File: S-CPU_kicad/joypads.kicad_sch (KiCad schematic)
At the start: 280 parts, among them U33 OR_2, U38 OR_2

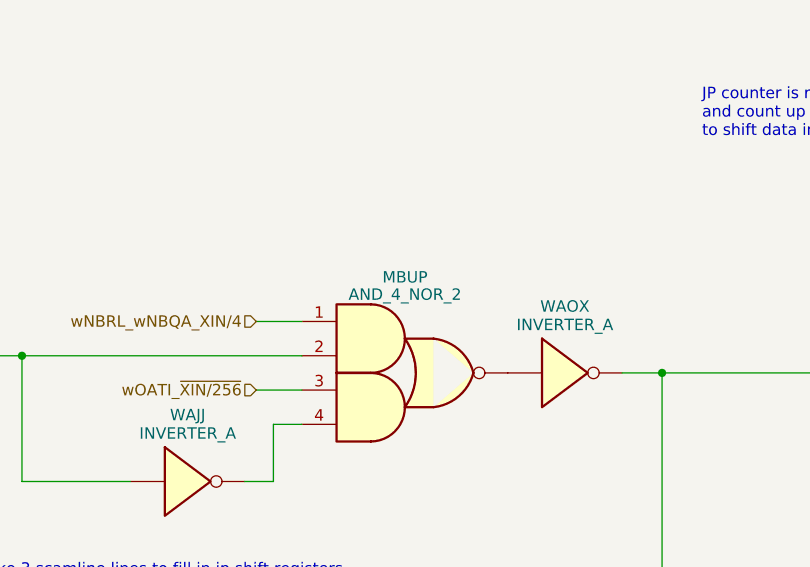
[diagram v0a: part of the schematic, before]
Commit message: Fixed complex gate names. Most fo the cells in the mul div section have been idnetified in SVG file.
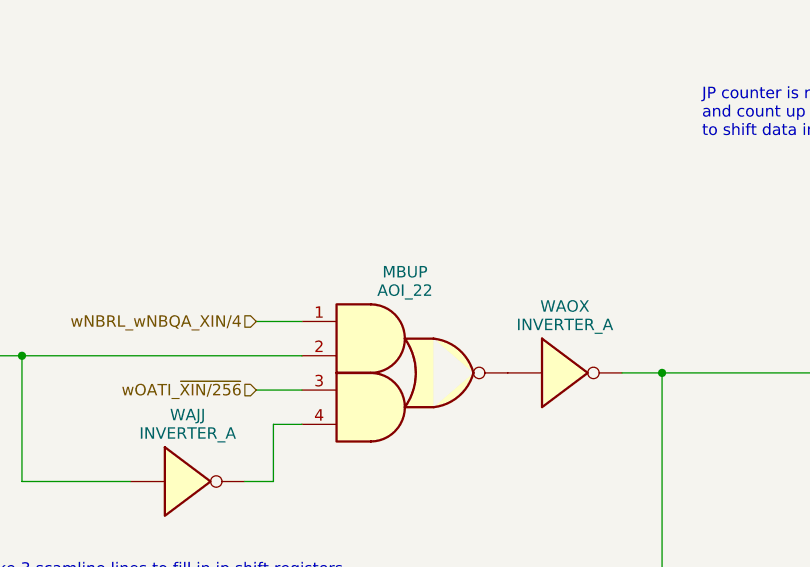
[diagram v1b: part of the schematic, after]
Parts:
- MBUP: value AND_4_NOR_2 -> AOI_22; symbol Ricoh_Cells:AND_2_AND_2_NOR_2 -> Ricoh_Cells:AOI_22
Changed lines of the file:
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@@
     )
   )
-  (symbol (lib_id "Ricoh_Cells:AND_2_AND_2_NOR_2") (at 226.06 92.71 0) (unit 1)
+  (symbol (lib_id "Ricoh_Cells:AOI_22") (at 226.06 92.71 0) (unit 1)
     (in_bom yes) (on_board yes) (dnp no) (fields_autoplaced)
-    (property "Reference" "MBUP" (at 229.8837 80.8101 0)
+    (property "Reference" "MBUP" (at 229.8837 80.24 0)
       (effects (font (size 1.27 1.27)))
     )
-    (property "Value" "AND_4_NOR_2" (at 229.8837 82.7311 0)
+    (property "Value" "AOI_22" (at 229.8837 82.288 0)
       (effects (font (size 1.27 1.27)))
     )
@@
         )
         (path "/ca9d3ca9-0297-4b98-a109-b7c162ccc5c3/c42cdb83-bc69-486b-820b-017180bd7612"
-          (reference "MBUP1") (unit 1)
+          (reference "WAMB") (unit 1)
         )
       )

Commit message: More MUL DIV section updates,
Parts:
- ABVA1: symbol Ricoh_Cells:TRI_BUF_IF1 -> Ricoh_Cells:TRI_BUF_IF0
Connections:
- net wMASS renamed wMASS_RST
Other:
- moved on the sheet: ODYR, VAAA, VAQL

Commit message: ADDR and DAT bus progress
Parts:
- ABVA1: value TRI_BUF_IF0 -> TRI_BUF_IF1; symbol Ricoh_Cells:TRI_BUF_IF0 -> Ricoh_Cells:TRI_BUF_IF1
- JP2I0: value IOBUF_A -> IOBUF_B; symbol Ricoh_Cells:IOBUF_A -> Ricoh_Cells:IOBUF_B
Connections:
- net +5V: now also JP2I0.4 (~{DRV}_HIGH), JP2I0.4 (~{DRV}_HIGH), JP2I0.4 (~{DRV}_HIGH), JP2I0.4 (~{DRV}_HIGH), JP2I0.4 (~{DRV}_HIGH), JP2I0.4 (~{DRV}_HIGH), JP2I0.4 (~{DRV}_HIGH), JP2I0.4 (~{DRV}_HIGH); no longer JP2I0.3 (~{DRV}_HIGH), JP2I0.3 (~{DRV}_HIGH), JP2I0.3 (~{DRV}_HIGH), JP2I0.3 (~{DRV}_HIGH), JP2I0.3 (~{DRV}_HIGH), JP2I0.3 (~{DRV}_HIGH), JP2I0.3 (~{DRV}_HIGH), JP2I0.3 (~{DRV}_HIGH)
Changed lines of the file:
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@@
     )
   )
-  (symbol (lib_id "Ricoh_Cells:IOBUF_A") (at 41.275 515.62 0) (unit 1)
+  (symbol (lib_id "Ricoh_Cells:IOBUF_B") (at 41.275 515.62 0) (unit 1)
     (in_bom yes) (on_board yes) (dnp no) (fields_autoplaced)
     (property "Reference" "JP2I0" (at 41.275 507.6571 0)
       (effects (font (size 1.27 1.27)))
     )
-    (property "Value" "IOBUF_A" (at 41.275 509.5781 0)
+    (property "Value" "IOBUF_B" (at 41.275 509.5781 0)
       (effects (font (size 1.27 1.27)))
     )
@@
     (pin "1")
     (pin "2")
-    (pin "3")
+    (pin "4")
     (instances
       (project "S-CPU"
@@
     )
   )
-  (symbol (lib_id "Ricoh_Cells:TRI_BUF_IF0") (at 626.11 98.425 0) (unit 1)
+  (symbol (lib_id "Ricoh_Cells:TRI_BUF_IF1") (at 626.11 98.425 0) (unit 1)
     (in_bom yes) (on_board yes) (dnp no) (fields_autoplaced)
     (property "Reference" "ABVA1" (at 626.11 103.767 0)
       (effects (font (size 1.27 1.27)))
     )
-    (property "Value" "TRI_BUF_IF0" (at 626.11 106.045 0)
+    (property "Value" "TRI_BUF_IF1" (at 626.11 106.045 0)
       (effects (font (size 1.27 1.27)))
     )
@@
     )
   )
-  (symbol (lib_id "Ricoh_Cells:IOBUF_A") (at 41.275 497.84 0) (unit 1)
+  (symbol (lib_id "Ricoh_Cells:IOBUF_B") (at 41.275 497.84 0) (unit 1)
     (in_bom yes) (on_board yes) (dnp no) (fields_autoplaced)
     (property "Reference" "JP2I0" (at 41.275 489.8771 0)
       (effects (font (size 1.27 1.27)))
     )
-    (property "Value" "IOBUF_A" (at 41.275 491.7981 0)
+    (property "Value" "IOBUF_B" (at 41.275 491.7981 0)
       (effects (font (size 1.27 1.27)))
     )
@@
     (pin "1")
     (pin "2")
-    (pin "3")
+    (pin "4")
     (instances
       (project "S-CPU"
@@
       (effects (font (size 1.27 1.27)) hide)
     )
-    (property "Datasheet" "http://iceboy.a-singer.de/doc/dmg_cells.html#obuf_a" (at 487.68 113.665 0)
+    (property "Datasheet" "" (at 487.68 113.665 0)
       (effects (font (size 1.27 1.27)) hide)
     )
@@
       (effects (font (size 1.27 1.27)) hide)
     )
-    (property "Datasheet" "http://iceboy.a-singer.de/doc/dmg_cells.html#ibuf" (at 709.93 309.245 0)
+    (property "Datasheet" "" (at 709.93 309.245 0)
       (effects (font (size 1.27 1.27)) hide)
     )
@@
       (effects (font (size 1.27 1.27)) hide)
     )
-    (property "Datasheet" "http://iceboy.a-singer.de/doc/dmg_cells.html#ibuf" (at 709.93 451.485 0)
+    (property "Datasheet" "" (at 709.93 451.485 0)
       (effects (font (size 1.27 1.27)) hide)
     )
@@
       (effects (font (size 1.27 1.27)) hide)
     )
-    (property "Datasheet" "http://iceboy.a-singer.de/doc/dmg_cells.html#ibuf" (at 709.93 475.615 0)
+    (property "Datasheet" "" (at 709.93 475.615 0)
       (effects (font (size 1.27 1.27)) hide)
     )
@@
       (effects (font (size 1.27 1.27)) hide)
     )
-    (property "Datasheet" "http://iceboy.a-singer.de/doc/dmg_cells.html#tri_buf_if0" (at 627.38 126.365 0)
+    (property "Datasheet" "http://iceboy.a-singer.de/doc/dmg_cells.html#tri_inv_if0" (at 627.38 126.365 0)
       (effects (font (size 1.27 1.27)) hide)
     )
@@
       (effects (font (size 1.27 1.27)) hide)
     )
-    (property "Datasheet" "http://iceboy.a-singer.de/doc/dmg_cells.html#ibuf" (at 709.93 427.355 0)
+    (property "Datasheet" "" (at 709.93 427.355 0)
       (effects (font (size 1.27 1.27)) hide)
     )
@@
     )
   )
-  (symbol (lib_id "Ricoh_Cells:IOBUF_A") (at 41.275 533.4 0) (unit 1)
+  (symbol (lib_id "Ricoh_Cells:IOBUF_B") (at 41.275 533.4 0) (unit 1)
     (in_bom yes) (on_board yes) (dnp no) (fields_autoplaced)
     (property "Reference" "JP2I0" (at 41.275 525.4371 0)
       (effects (font (size 1.27 1.27)))
     )
-    (property "Value" "IOBUF_A" (at 41.275 527.3581 0)
+    (property "Value" "IOBUF_B" (at 41.275 527.3581 0)
       (effects (font (size 1.27 1.27)))
     )
@@
     (pin "1")
     (pin "2")
-    (pin "3")
+    (pin "4")
     (instances
       (project "S-CPU"
@@
       (effects (font (size 1.27 1.27)) hide)
     )
-    (property "Datasheet" "http://iceboy.a-singer.de/doc/dmg_cells.html#tri_buf_if0" (at 627.38 144.145 0)
+    (property "Datasheet" "http://iceboy.a-singer.de/doc/dmg_cells.html#tri_inv_if0" (at 627.38 144.145 0)
       (effects (font (size 1.27 1.27)) hide)
     )
@@
     )
   )
-  (symbol (lib_id "Ricoh_Cells:IOBUF_A") (at 41.275 480.06 0) (unit 1)
+  (symbol (lib_id "Ricoh_Cells:IOBUF_B") (at 41.275 480.06 0) (unit 1)
     (in_bom yes) (on_board yes) (dnp no) (fields_autoplaced)
     (property "Reference" "JP2I0" (at 41.275 472.0971 0)
       (effects (font (size 1.27 1.27)))
     )
-    (property "Value" "IOBUF_A" (at 41.275 474.0181 0)
+    (property "Value" "IOBUF_B" (at 41.275 474.0181 0)
       (effects (font (size 1.27 1.27)))
     )
@@
     (pin "1")
     (pin "2")
-    (pin "3")
+    (pin "4")
     (instances
       (project "S-CPU"
@@
       (effects (font (size 1.27 1.27)) hide)
     )
-    (property "Datasheet" "http://iceboy.a-singer.de/doc/dmg_cells.html#obuf_a" (at 487.68 127.635 0)
+    (property "Datasheet" "" (at 487.68 127.635 0)
       (effects (font (size 1.27 1.27)) hide)
     )
@@
       (effects (font (size 1.27 1.27)) hide)
     )
-    (property "Datasheet" "http://iceboy.a-singer.de/doc/dmg_cells.html#ibuf" (at 709.93 333.375 0)
+    (property "Datasheet" "" (at 709.93 333.375 0)
       (effects (font (size 1.27 1.27)) hide)
     )
@@
     )
   )
-  (symbol (lib_id "Ricoh_Cells:IOBUF_A") (at 41.275 551.18 0) (unit 1)
+  (symbol (lib_id "Ricoh_Cells:IOBUF_B") (at 41.275 551.18 0) (unit 1)
     (in_bom yes) (on_board yes) (dnp no) (fields_autoplaced)
     (property "Reference" "JP2I0" (at 41.275 543.2171 0)
       (effects (font (size 1.27 1.27)))
     )
-    (property "Value" "IOBUF_A" (at 41.275 545.1381 0)
+    (property "Value" "IOBUF_B" (at 41.275 545.1381 0)
       (effects (font (size 1.27 1.27)))
     )
@@
     (pin "1")
     (pin "2")
-    (pin "3")
+    (pin "4")
     (instances
       (project "S-CPU"
@@
     )
   )
-  (symbol (lib_id "Ricoh_Cells:IOBUF_A") (at 41.275 444.5 0) (unit 1)
+  (symbol (lib_id "Ricoh_Cells:IOBUF_B") (at 41.275 444.5 0) (unit 1)
     (in_bom yes) (on_board yes) (dnp no) (fields_autoplaced)
     (property "Reference" "JP2I0" (at 41.275 436.5371 0)
       (effects (font (size 1.27 1.27)))
     )
-    (property "Value" "IOBUF_A" (at 41.275 438.4581 0)
+    (property "Value" "IOBUF_B" (at 41.275 438.4581 0)
       (effects (font (size 1.27 1.27)))
     )
@@
     (pin "1")
     (pin "2")
-    (pin "3")
+    (pin "4")
     (instances
       (project "S-CPU"
@@
       (effects (font (size 1.27 1.27)) hide)
     )
-    (property "Datasheet" "http://iceboy.a-singer.de/doc/dmg_cells.html#ibuf" (at 709.93 403.225 0)
+    (property "Datasheet" "" (at 709.93 403.225 0)
       (effects (font (size 1.27 1.27)) hide)
     )
@@
       (effects (font (size 1.27 1.27)) hide)
     )
-    (property "Datasheet" "http://iceboy.a-singer.de/doc/dmg_cells.html#obuf_a" (at 708.025 175.895 0)
+    (property "Datasheet" "" (at 708.025 175.895 0)
       (effects (font (size 1.27 1.27)) hide)
     )
@@
     )
   )
-  (symbol (lib_id "Ricoh_Cells:IOBUF_A") (at 41.275 462.28 0) (unit 1)
+  (symbol (lib_id "Ricoh_Cells:IOBUF_B") (at 41.275 462.28 0) (unit 1)
     (in_bom yes) (on_board yes) (dnp no) (fields_autoplaced)
     (property "Reference" "JP2I0" (at 41.275 454.3171 0)
       (effects (font (size 1.27 1.27)))
     )
-    (property "Value" "IOBUF_A" (at 41.275 456.2381 0)
+    (property "Value" "IOBUF_B" (at 41.275 456.2381 0)
       (effects (font (size 1.27 1.27)))
     )
@@
     (pin "1")
     (pin "2")
-    (pin "3")
+    (pin "4")
     (instances
       (project "S-CPU"
@@
     )
   )
-  (symbol (lib_id "Ricoh_Cells:IOBUF_A") (at 41.275 426.72 0) (unit 1)
+  (symbol (lib_id "Ricoh_Cells:IOBUF_B") (at 41.275 426.72 0) (unit 1)
     (in_bom yes) (on_board yes) (dnp no) (fields_autoplaced)
     (property "Reference" "JP2I0" (at 41.275 418.7571 0)
       (effects (font (size 1.27 1.27)))
     )
-    (property "Value" "IOBUF_A" (at 41.275 420.6781 0)
+    (property "Value" "IOBUF_B" (at 41.275 420.6781 0)
       (effects (font (size 1.27 1.27)))
     )
@@
     (pin "1")
     (pin "2")
-    (pin "3")
+    (pin "4")
     (instances
       (project "S-CPU"
@@
       (effects (font (size 1.27 1.27)) hide)
     )
-    (property "Datasheet" "http://iceboy.a-singer.de/doc/dmg_cells.html#obuf_a" (at 708.025 208.915 0)
+    (property "Datasheet" "" (at 708.025 208.915 0)
       (effects (font (size 1.27 1.27)) hide)
     )
@@
       (effects (font (size 1.27 1.27)) hide)
     )
-    (property "Datasheet" "http://iceboy.a-singer.de/doc/dmg_cells.html#obuf_a" (at 708.025 192.405 0)
+    (property "Datasheet" "" (at 708.025 192.405 0)
       (effects (font (size 1.27 1.27)) hide)
     )
@@
       (effects (font (size 1.27 1.27)) hide)
     )
-    (property "Datasheet" "http://iceboy.a-singer.de/doc/dmg_cells.html#ibuf" (at 709.93 379.095 0)
+    (property "Datasheet" "" (at 709.93 379.095 0)
       (effects (font (size 1.27 1.27)) hide)
     )

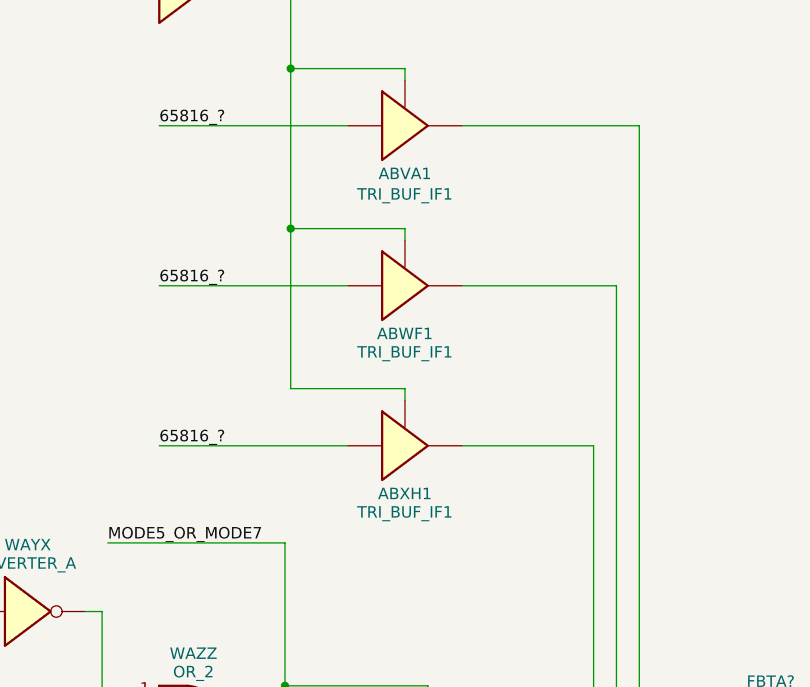
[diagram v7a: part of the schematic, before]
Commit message: Some cells had the wrong ID in the producter remainder sheet. Allocation of new names in spreadsheet for cells in the DMA section
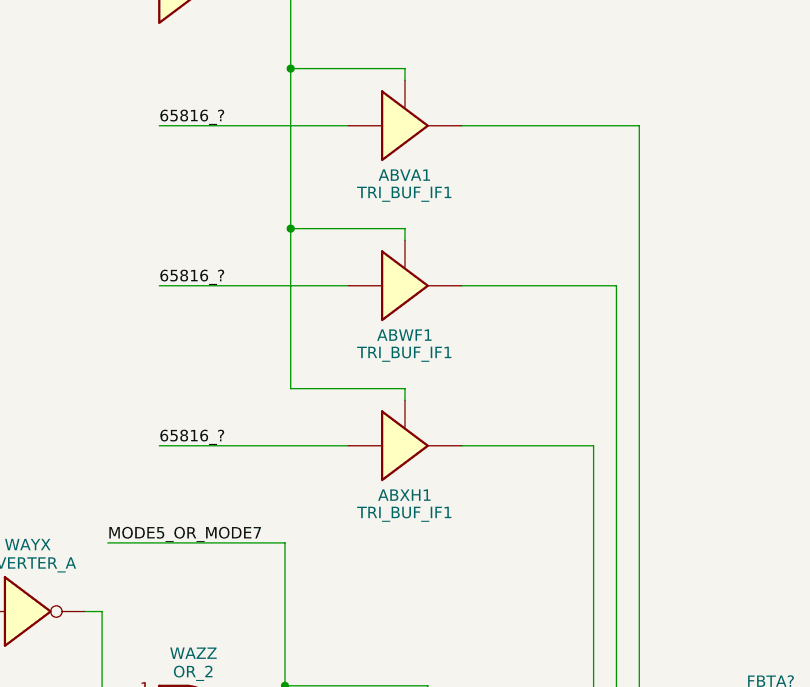
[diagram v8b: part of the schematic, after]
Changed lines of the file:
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@@
   (symbol (lib_id "Ricoh_Cells:TRI_BUF_IF1") (at 626.11 98.425 0) (unit 1)
     (in_bom yes) (on_board yes) (dnp no) (fields_autoplaced)
-    (property "Reference" "ABVA1" (at 626.11 103.767 0)
+    (property "Reference" "ABVA1" (at 626.11 103.9551 0)
       (effects (font (size 1.27 1.27)))
     )
-    (property "Value" "TRI_BUF_IF1" (at 626.11 106.045 0)
+    (property "Value" "TRI_BUF_IF1" (at 626.11 105.8785 0)
       (effects (font (size 1.27 1.27)))
     )
@@
         )
         (path "/ca9d3ca9-0297-4b98-a109-b7c162ccc5c3/c42cdb83-bc69-486b-820b-017180bd7612"
-          (reference "ODYN") (unit 1)
+          (reference "ODYN0") (unit 1)
         )
       )
@@
   (symbol (lib_id "Ricoh_Cells:TRI_BUF_IF1") (at 626.11 116.205 0) (unit 1)
     (in_bom yes) (on_board yes) (dnp no) (fields_autoplaced)
-    (property "Reference" "ABWF1" (at 626.11 121.547 0)
+    (property "Reference" "ABWF1" (at 626.11 121.7351 0)
       (effects (font (size 1.27 1.27)))
     )
-    (property "Value" "TRI_BUF_IF1" (at 626.11 123.595 0)
+    (property "Value" "TRI_BUF_IF1" (at 626.11 123.6585 0)
       (effects (font (size 1.27 1.27)))
     )
@@
       (effects (font (size 1.27 1.27)) hide)
     )
-    (property "Datasheet" "http://iceboy.a-singer.de/doc/dmg_cells.html#tri_inv_if0" (at 627.38 126.365 0)
+    (property "Datasheet" "http://iceboy.a-singer.de/doc/dmg_cells.html#tri_buf_if0" (at 627.38 126.365 0)
       (effects (font (size 1.27 1.27)) hide)
     )
@@
         )
         (path "/ca9d3ca9-0297-4b98-a109-b7c162ccc5c3/c42cdb83-bc69-486b-820b-017180bd7612"
-          (reference "ODYO") (unit 1)
+          (reference "ODYN1") (unit 1)
         )
       )
@@
   (symbol (lib_id "Ricoh_Cells:TRI_BUF_IF1") (at 626.11 133.985 0) (unit 1)
     (in_bom yes) (on_board yes) (dnp no) (fields_autoplaced)
-    (property "Reference" "ABXH1" (at 626.11 139.327 0)
+    (property "Reference" "ABXH1" (at 626.11 139.5151 0)
       (effects (font (size 1.27 1.27)))
     )
-    (property "Value" "TRI_BUF_IF1" (at 626.11 141.375 0)
+    (property "Value" "TRI_BUF_IF1" (at 626.11 141.4385 0)
       (effects (font (size 1.27 1.27)))
     )
@@
       (effects (font (size 1.27 1.27)) hide)
     )
-    (property "Datasheet" "http://iceboy.a-singer.de/doc/dmg_cells.html#tri_inv_if0" (at 627.38 144.145 0)
+    (property "Datasheet" "http://iceboy.a-singer.de/doc/dmg_cells.html#tri_buf_if0" (at 627.38 144.145 0)
       (effects (font (size 1.27 1.27)) hide)
     )
@@
         )
         (path "/ca9d3ca9-0297-4b98-a109-b7c162ccc5c3/c42cdb83-bc69-486b-820b-017180bd7612"
-          (reference "ODYP") (unit 1)
+          (reference "ODYN2") (unit 1)
         )
       )
